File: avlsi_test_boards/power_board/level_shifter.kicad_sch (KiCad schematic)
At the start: 7 parts, among them U13 SN74LVC16T245DLR

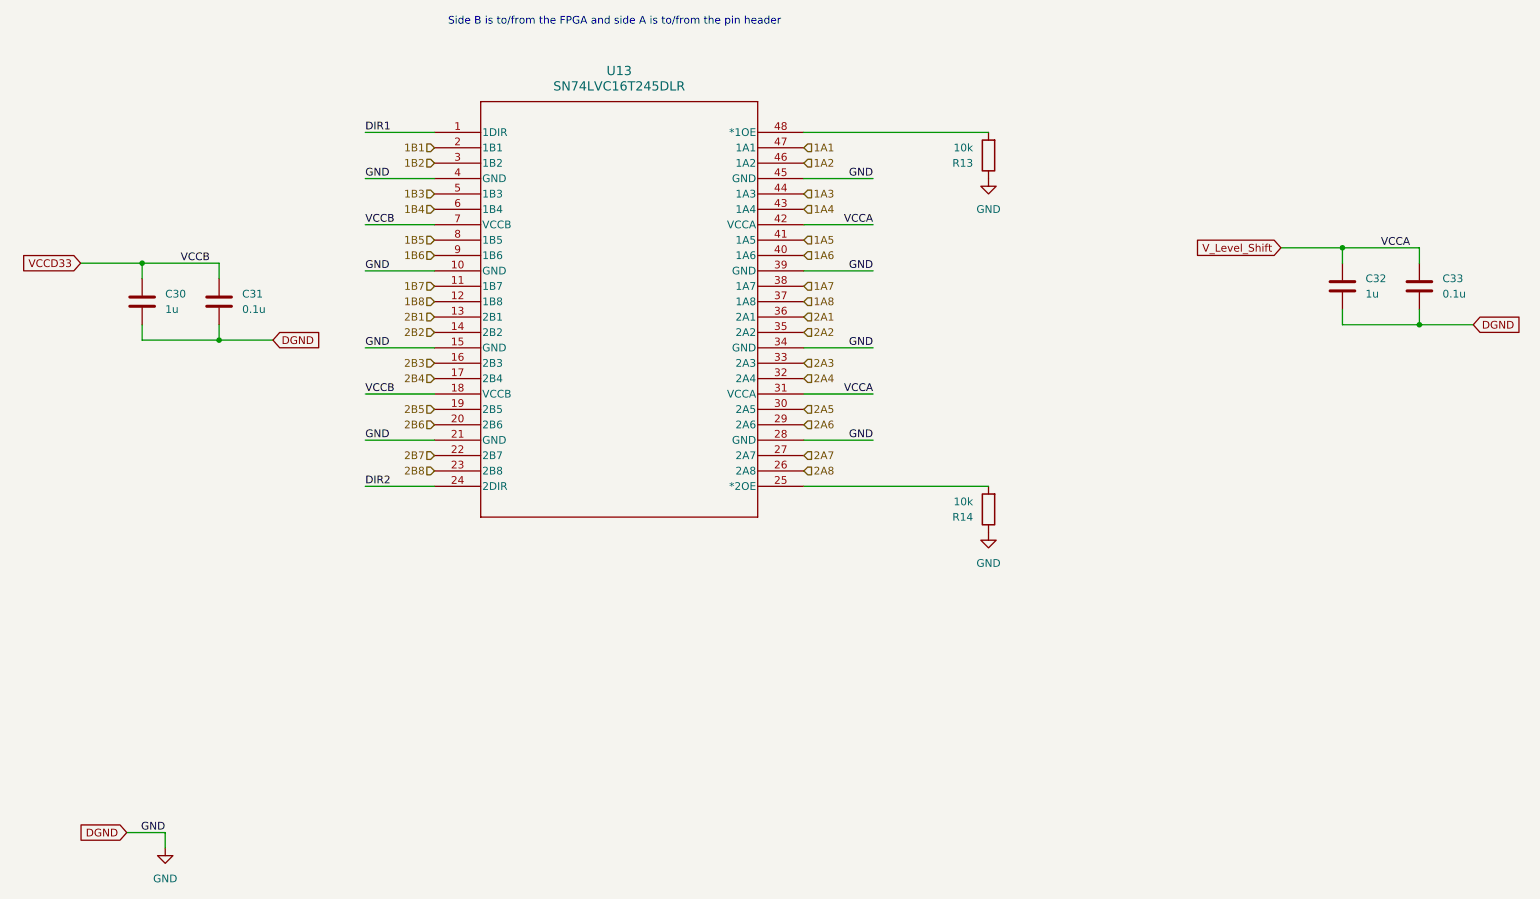
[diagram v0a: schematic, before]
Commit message: Update schematic and initial layout for pcb
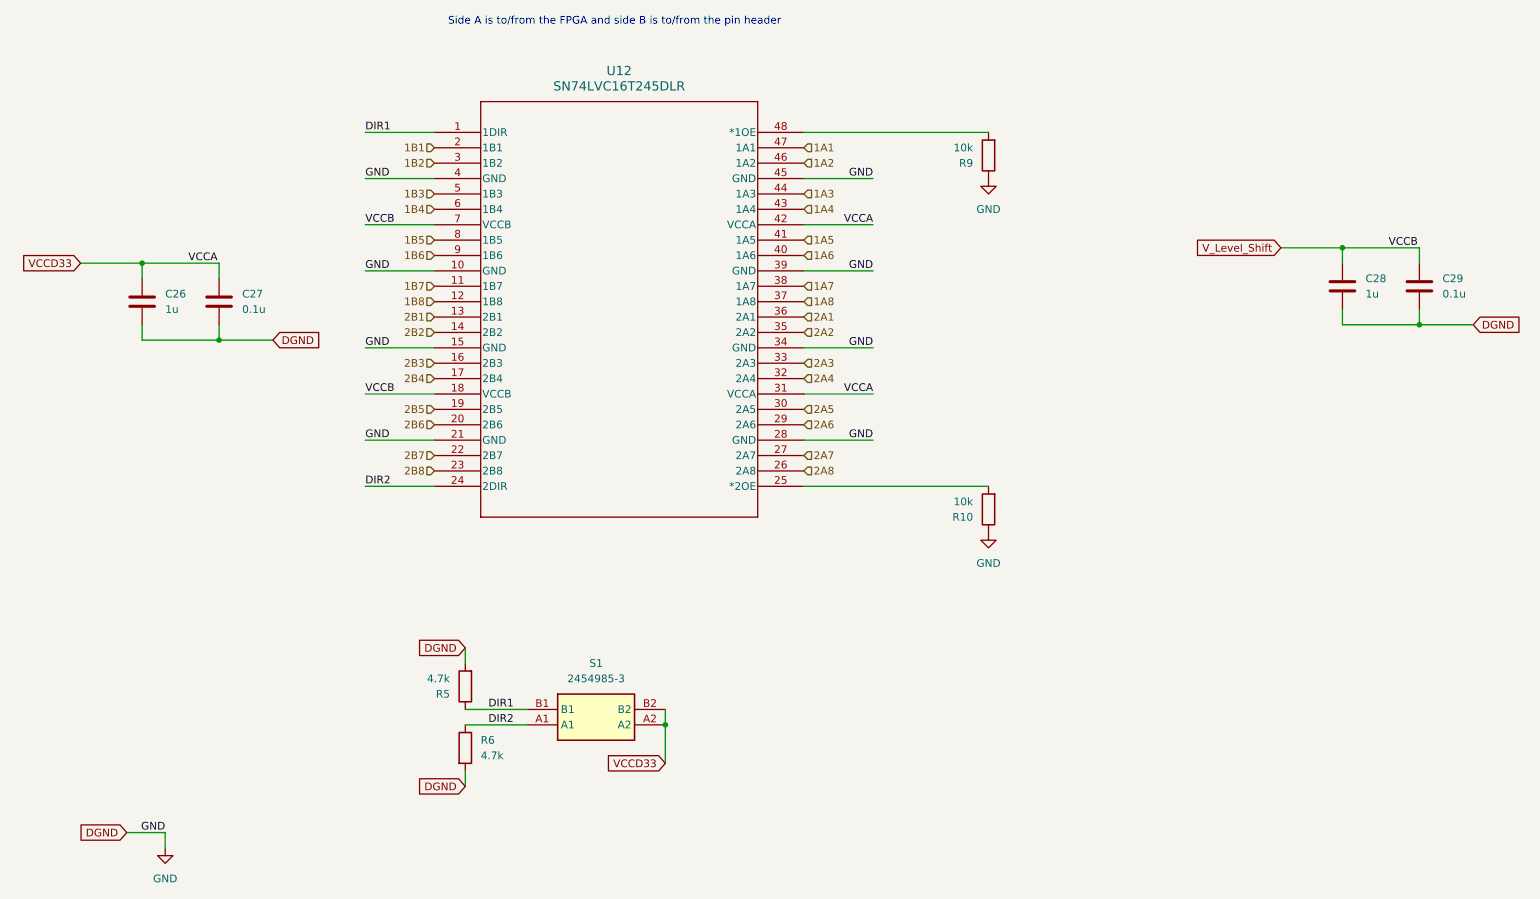
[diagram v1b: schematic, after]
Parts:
- added R5, R6: 4.7k, Resistor_SMD:R_0805_2012Metric, symbol Device:R
- added S1: 2454985-3, 2_DS:24549853, symbol 2_DIP:2454985-3
- renumbered C30 to C26, C31 to C27, C32 to C28, C33 to C29, R14 to R10, R13 to R9, U13 to U12
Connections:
- net DIR1: now also R5.1, S1.B1
- net DIR2: now also R6.1, S1.A1
- net GND: now also R5.2, R6.2
- net VCCD33: now also U12.31 (VCCA), U12.42 (VCCA), S1.A2, S1.B2; no longer U12.18 (VCCB), U12.7 (VCCB)
- net V_Level_Shift: now also U12.18 (VCCB), U12.7 (VCCB); no longer U12.31 (VCCA), U12.42 (VCCA)
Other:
- note added: "Side A is to/from the FPGA and side B is to/from the pin header"
- note removed: "Side B is to/from the FPGA and side A is to/from the pin header"

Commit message: Add updated symbol
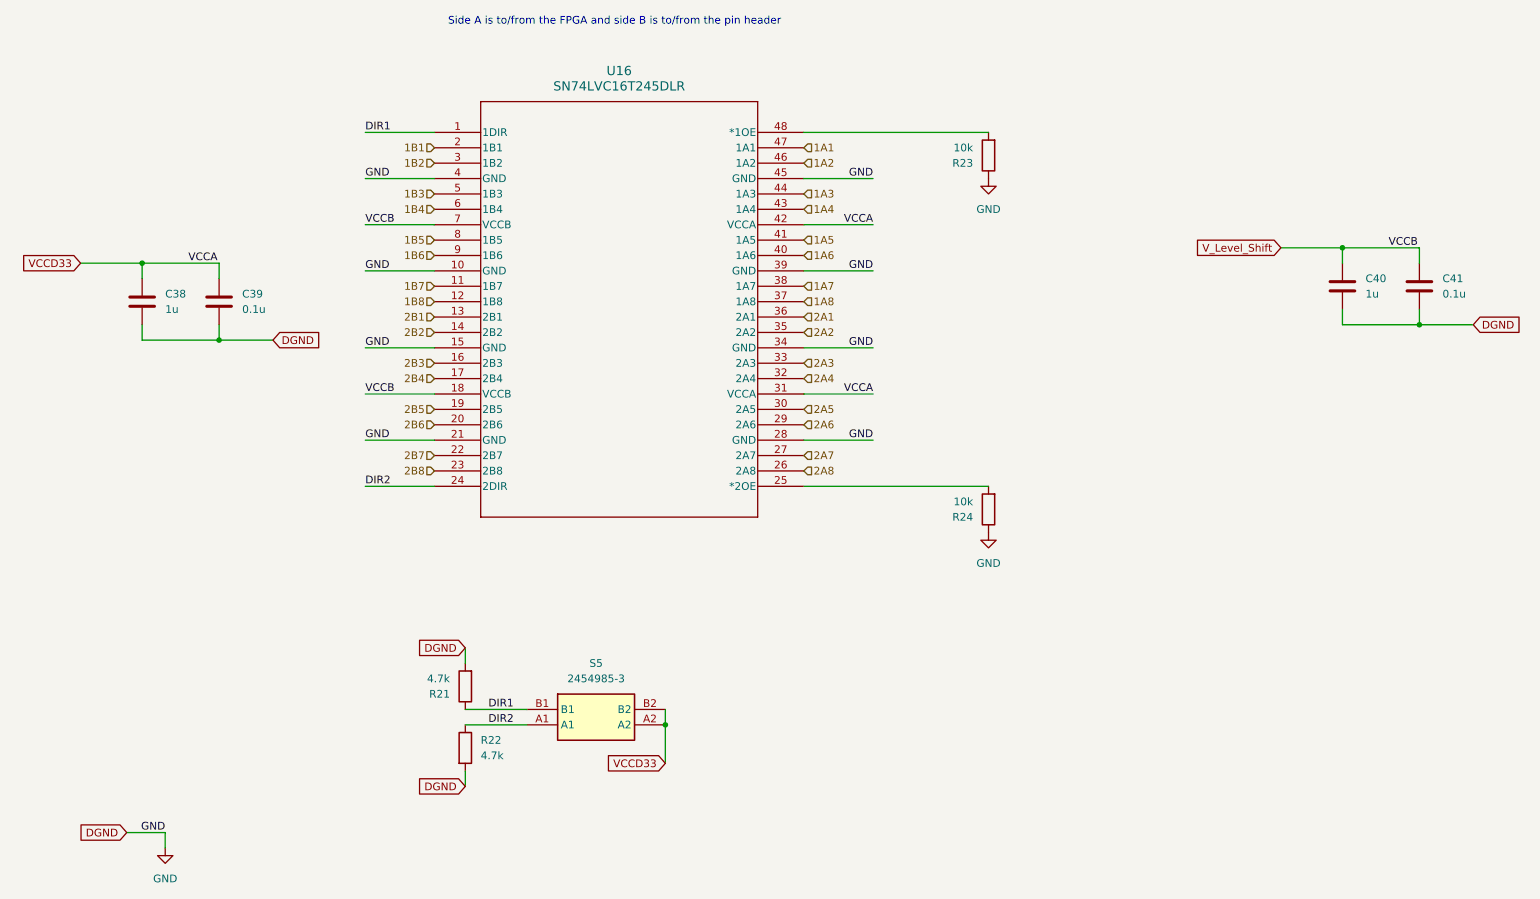
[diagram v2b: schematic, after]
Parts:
- renumbered C26 to C38, C27 to C39, C28 to C40, C29 to C41, R5 to R21, R6 to R22, R9 to R23, R10 to R24, S1 to S5, U12 to U16
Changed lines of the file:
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@@
 		(dnp no)
 		(fields_autoplaced yes)
-		(property "Reference" "S1"
+		(property "Reference" "S5"
 			(at 113.03 151.13 0)
 			(effects
@@
 		(dnp no)
 		(fields_autoplaced yes)
-		(property "Reference" "#PWR05"
+		(property "Reference" "#PWR014"
 			(at 177.8 77.47 0)
 			(effects
@@
 		(dnp no)
 		(fields_autoplaced yes)
-		(property "Reference" "C29"
+		(property "Reference" "C41"
 			(at 252.73 87.6299 0)
 			(effects
@@
 		(dnp no)
 		(fields_autoplaced yes)
-		(property "Reference" "C26"
+		(property "Reference" "C38"
 			(at 41.91 90.1699 0)
 			(effects
@@
 		(dnp no)
 		(fields_autoplaced yes)
-		(property "Reference" "U12"
+		(property "Reference" "U16"
 			(at 116.84 53.34 0)
 			(effects
@@
 		(dnp no)
 		(fields_autoplaced yes)
-		(property "Reference" "C27"
+		(property "Reference" "C39"
 			(at 54.61 90.1699 0)
 			(effects
@@
 		(dnp no)
 		(fields_autoplaced yes)
-		(property "Reference" "C28"
+		(property "Reference" "C40"
 			(at 240.03 87.6299 0)
 			(effects
@@
 		(dnp no)
 		(fields_autoplaced yes)
-		(property "Reference" "R6"
+		(property "Reference" "R22"
 			(at 93.98 163.8299 0)
 			(effects
@@
 		(dnp no)
 		(fields_autoplaced yes)
-		(property "Reference" "R10"
+		(property "Reference" "R24"
 			(at 175.26 127.0001 0)
 			(effects
@@
 		(dnp no)
 		(fields_autoplaced yes)
-		(property "Reference" "R9"
+		(property "Reference" "R23"
 			(at 175.26 68.5801 0)
 			(effects
@@
 		(dnp no)
 		(fields_autoplaced yes)
-		(property "Reference" "#PWR06"
+		(property "Reference" "#PWR015"
 			(at 177.8 135.89 0)
 			(effects
@@
 		(dnp no)
 		(fields_autoplaced yes)
-		(property "Reference" "#PWR04"
+		(property "Reference" "#PWR013"
 			(at 41.91 187.96 0)
 			(effects
@@
 		(dnp no)
 		(fields_autoplaced yes)
-		(property "Reference" "R5"
+		(property "Reference" "R21"
 			(at 88.9 156.2101 0)
 			(effects

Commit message: Update schematic
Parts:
- removed R21, R22: 4.7k, Resistor_SMD:R_0805_2012Metric, symbol Device:R
- removed S5: 2454985-3, 2_DS:24549853, symbol 2_DIP:2454985-3
- renumbered C38 to C46, C39 to C47, C40 to C48, C41 to C49, R23 to R30, R24 to R31, U16 to U19
